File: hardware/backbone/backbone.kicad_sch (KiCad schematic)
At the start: 71 parts, among them J1 M20-7810645R, J140 M20-7810645R, J2 FROM_PREVIOUS, J3 M20-7810645R, J4 SM04B-SRSS-TB(LF)(SN), J5 FH12-24S-0.5SH(55), J9 TO NEXT, Q2 AO3401A, U1 ESP32-S3-WROOM-1_1U_FlexyPin_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, U10 ME6211C15M5G-N, U2 SN65HVD230DR, U3 HC-TYPE-C-16P-01A, U4 AP2112K-3.3TRG1, U5 AP2112K-3.3TRG1, U8 G3VM-61VY3, U9 ME6211C28M5G-N

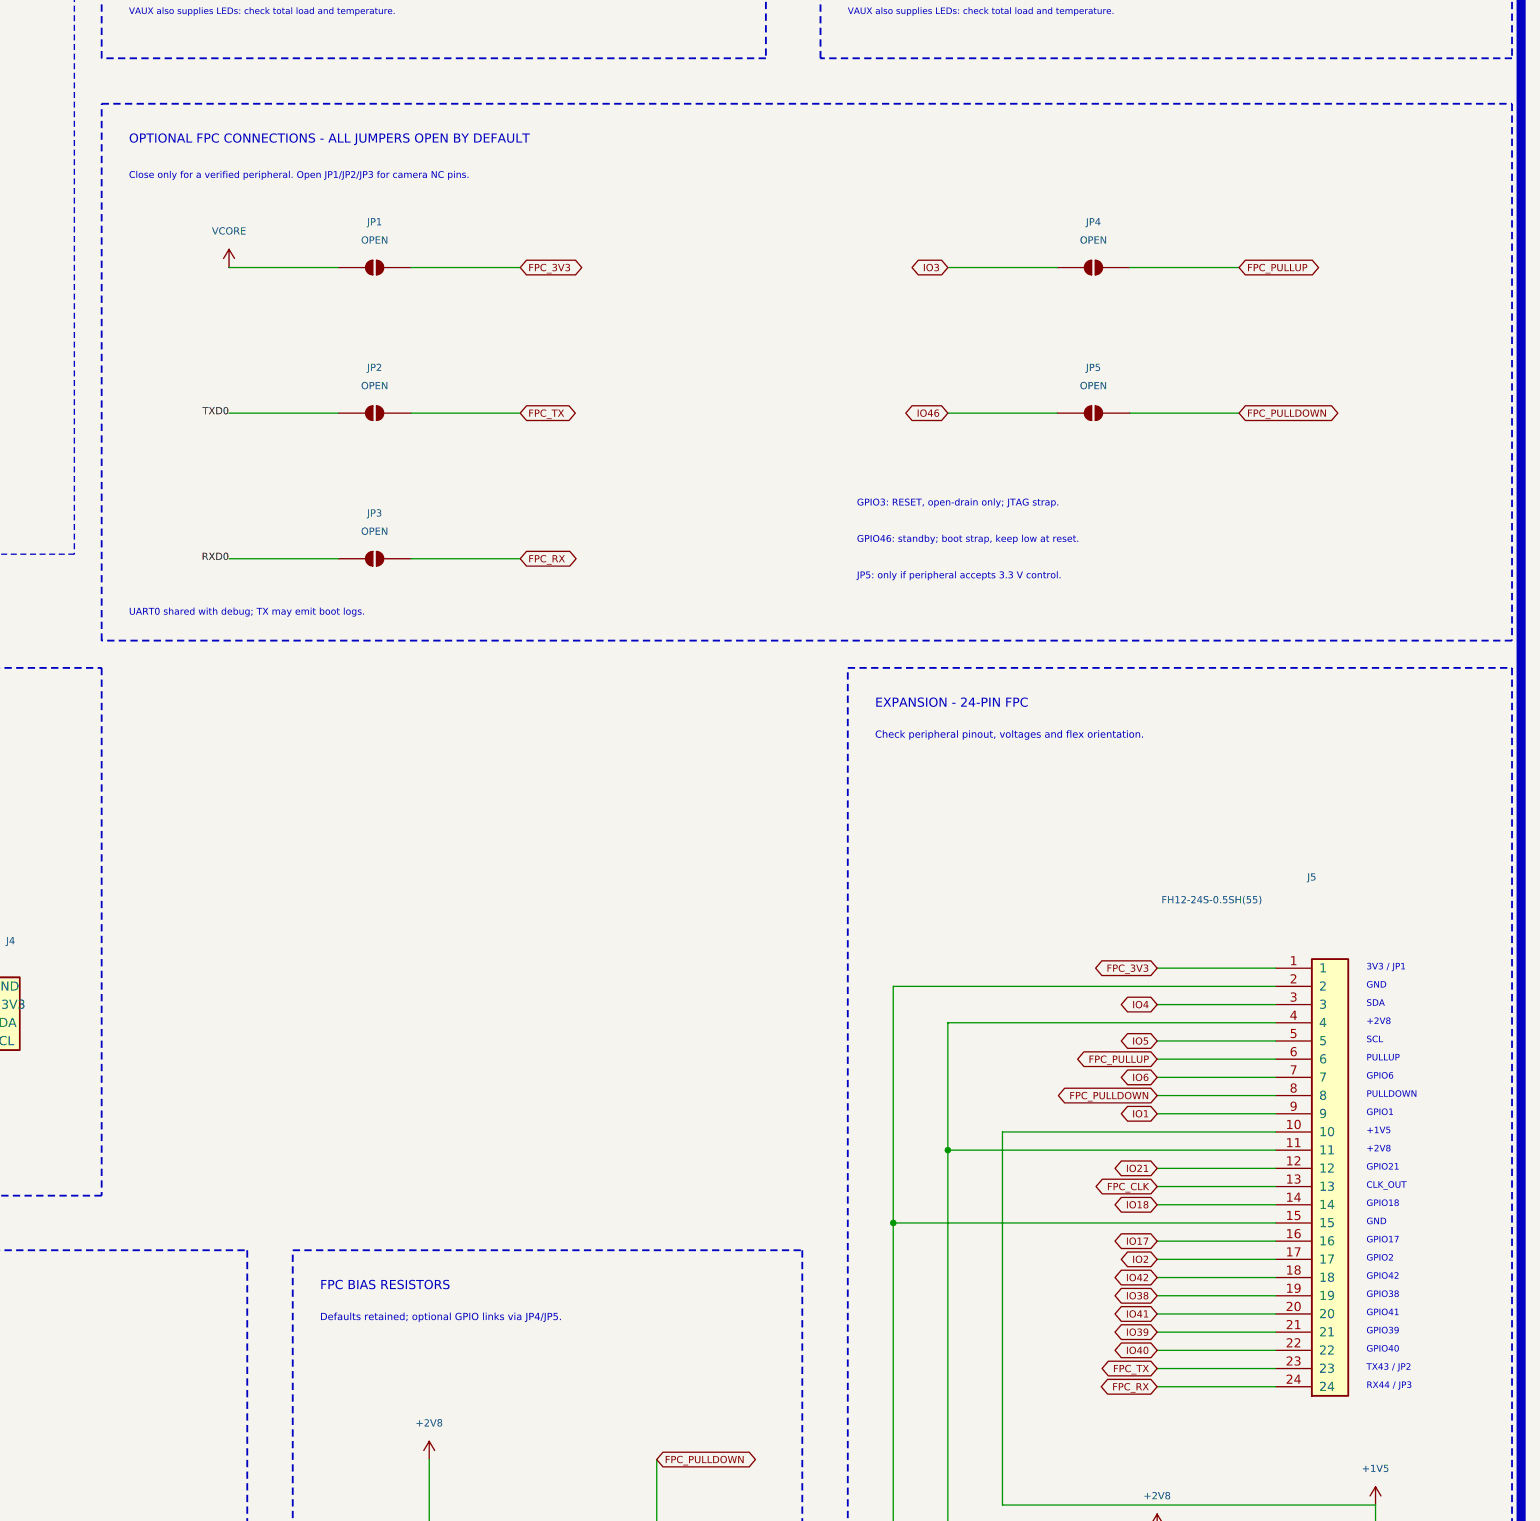
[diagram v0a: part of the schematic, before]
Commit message: Replace optional FPC solder jumpers with compact DNP zero-ohm links
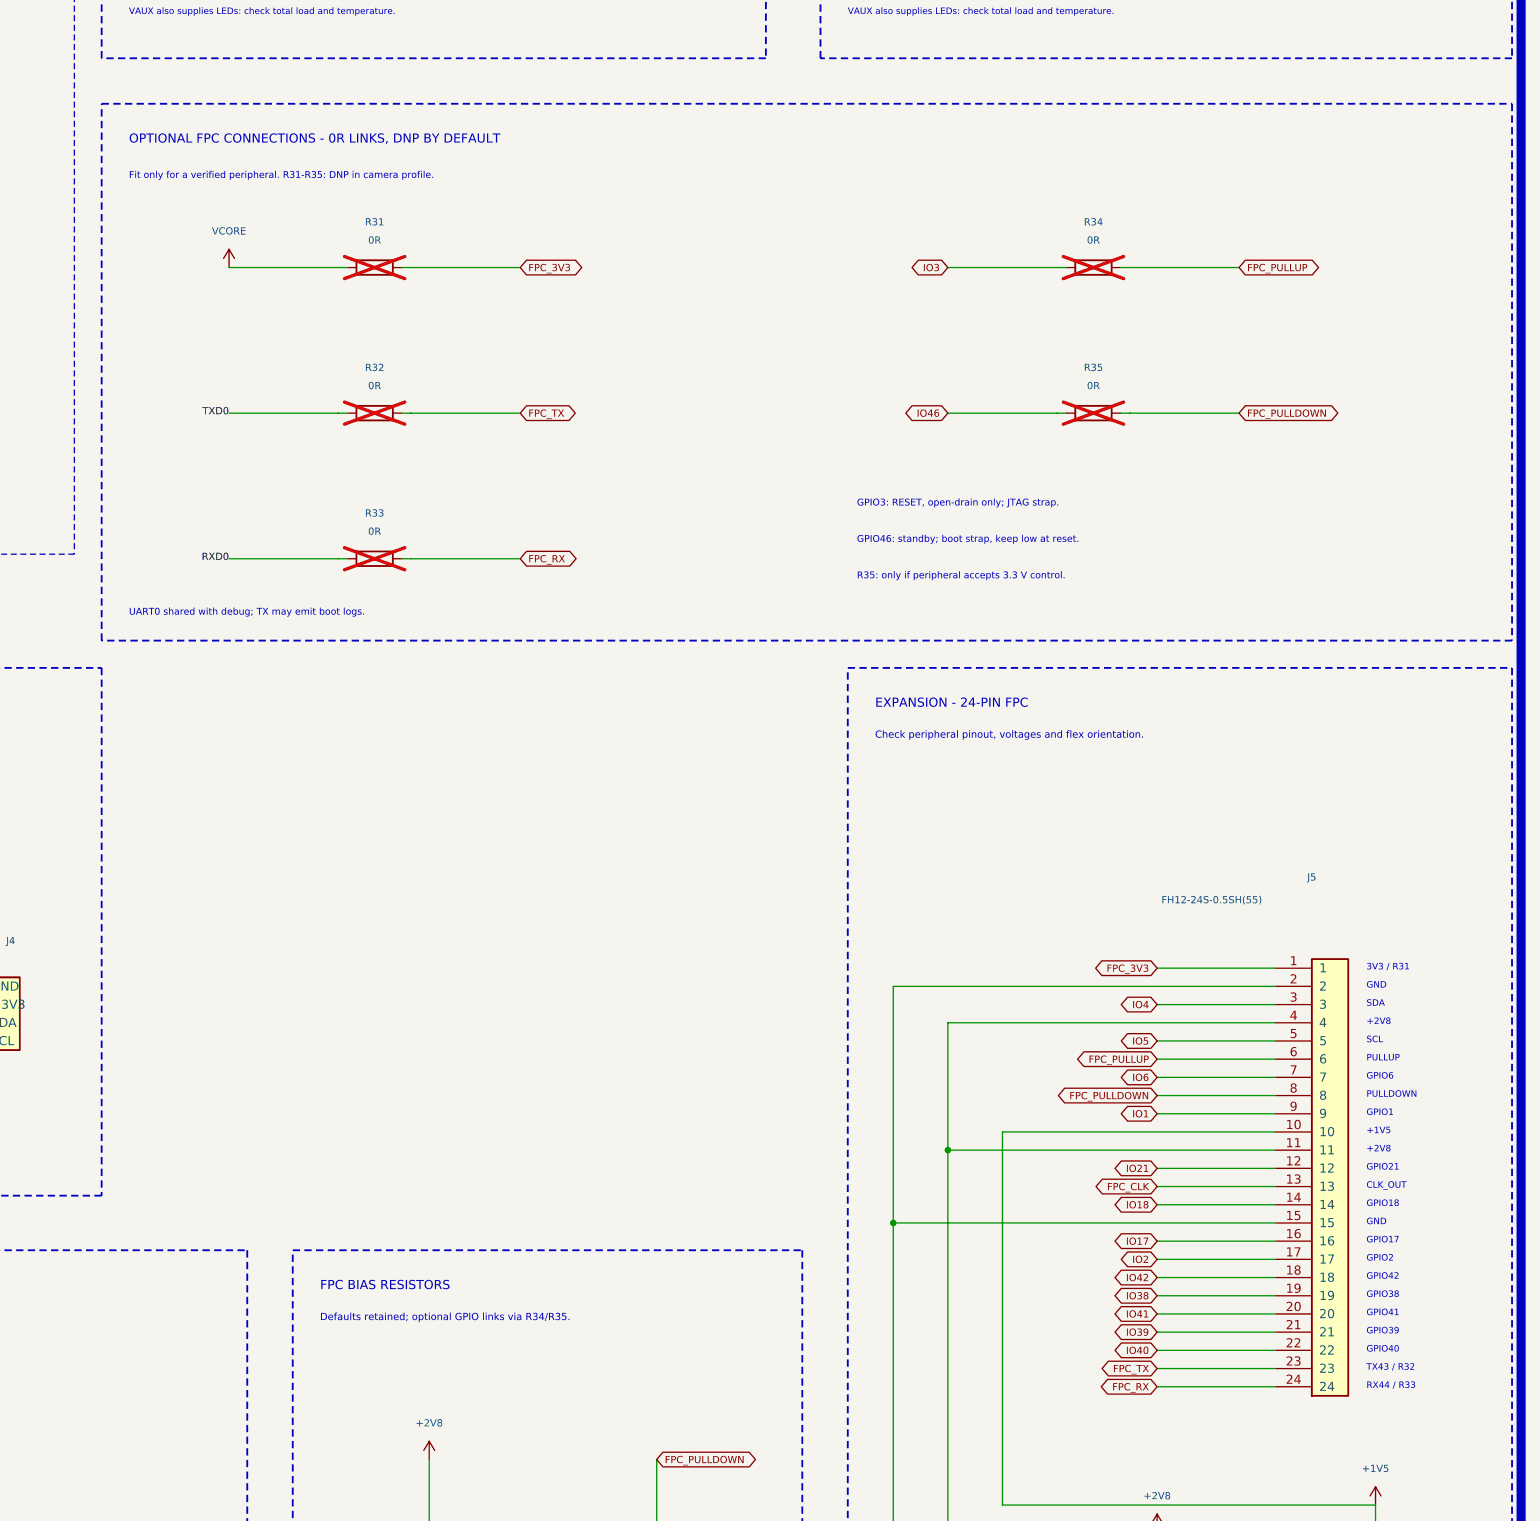
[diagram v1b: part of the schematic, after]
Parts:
- R31: renamed from JP1; value OPEN -> 0R; footprint Jumper:SolderJumper-2_P1.3mm_Open_Pad1.0x1.5mm -> Resistor_SMD:R_0402_1005Metric; symbol Jumper:SolderJumper_2_Open -> Device:R; now not fitted; now in the parts list
- R32: renamed from JP2; value OPEN -> 0R; footprint Jumper:SolderJumper-2_P1.3mm_Open_Pad1.0x1.5mm -> Resistor_SMD:R_0402_1005Metric; symbol Jumper:SolderJumper_2_Open -> Device:R; now not fitted; now in the parts list
- R33: renamed from JP3; value OPEN -> 0R; footprint Jumper:SolderJumper-2_P1.3mm_Open_Pad1.0x1.5mm -> Resistor_SMD:R_0402_1005Metric; symbol Jumper:SolderJumper_2_Open -> Device:R; now not fitted; now in the parts list
- R34: renamed from JP4; value OPEN -> 0R; footprint Jumper:SolderJumper-2_P1.3mm_Open_Pad1.0x1.5mm -> Resistor_SMD:R_0402_1005Metric; symbol Jumper:SolderJumper_2_Open -> Device:R; now not fitted; now in the parts list
- R35: renamed from JP5; value OPEN -> 0R; footprint Jumper:SolderJumper-2_P1.3mm_Open_Pad1.0x1.5mm -> Resistor_SMD:R_0402_1005Metric; symbol Jumper:SolderJumper_2_Open -> Device:R; now not fitted; now in the parts list
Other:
- note added: "3V3 / R31"
- note added: "Defaults retained; optional GPIO links via R34/R35."
- note added: "Fit only for a verified peripheral. R31-R35: DNP in camera profile."
- note added: "OPTIONAL FPC CONNECTIONS - 0R LINKS, DNP BY DEFAULT"
- note added: "R35: only if peripheral accepts 3.3 V control."
- note added: "RX44 / R33"
- note added: "TX43 / R32"
- note removed: "3V3 / JP1"
- note removed: "Close only for a verified peripheral. Open JP1/JP2/JP3 for camera NC pins."
- note removed: "Defaults retained; optional GPIO links via JP4/JP5."
- note removed: "JP5: only if peripheral accepts 3.3 V control."
- note removed: "OPTIONAL FPC CONNECTIONS - ALL JUMPERS OPEN BY DEFAULT"
- note removed: "RX44 / JP3"
- note removed: "TX43 / JP2"

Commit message: Use hand-solder 0603 links and document camera module compatibility
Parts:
- R31, R32, R33, R34, R35: footprint Resistor_SMD:R_0402_1005Metric -> Resistor_SMD:R_0603_1608Metric_Pad0.98x0.95mm_HandSolder
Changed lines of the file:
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@@
     )
   )
-  (property "Footprint" "Resistor_SMD:R_0402_1005Metric"
+  (property "Footprint" "Resistor_SMD:R_0603_1608Metric_Pad0.98x0.95mm_HandSolder"
     (at 420.37 124.46 0)
     (effects
@@
     )
   )
-  (property "Footprint" "Resistor_SMD:R_0402_1005Metric"
+  (property "Footprint" "Resistor_SMD:R_0603_1608Metric_Pad0.98x0.95mm_HandSolder"
     (at 420.37 144.78 0)
     (effects
@@
     )
   )
-  (property "Footprint" "Resistor_SMD:R_0402_1005Metric"
+  (property "Footprint" "Resistor_SMD:R_0603_1608Metric_Pad0.98x0.95mm_HandSolder"
     (at 420.37 165.1 0)
     (effects
@@
     )
   )
-  (property "Footprint" "Resistor_SMD:R_0402_1005Metric"
+  (property "Footprint" "Resistor_SMD:R_0603_1608Metric_Pad0.98x0.95mm_HandSolder"
     (at 520.7 124.46 0)
     (effects
@@
     )
   )
-  (property "Footprint" "Resistor_SMD:R_0402_1005Metric"
+  (property "Footprint" "Resistor_SMD:R_0603_1608Metric_Pad0.98x0.95mm_HandSolder"
     (at 520.7 144.78 0)
     (effects

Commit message: Update V3 LED layout for hand-formed MINI-E and solid FR4 windows
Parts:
- removed D4: SS54_C22452, SpaghettiLAB:SMA_L4.4-W2.8-LS5.4-R-RD, symbol SpaghettiLAB:SS54_C22452
- removed R20, R23: 5.1k, SpaghettiLAB:R0603, symbol Device:R
- removed USB1: TYPEC-324G-BCP24, SpaghettiLAB:USB-C-SMD_TYPEC-324G-BCP24, symbol SpaghettiLAB:TYPEC-324G-BCP24
- added D6: SS54_C22452, SpaghettiLAB:SMA_L4.4-W2.8-LS5.4-R-RD, symbol SpaghettiLAB:SS54_C22452
- added R22, R27: 5.1k, SpaghettiLAB:R0603, symbol Device:R
- LED1, LED2, LED3, LED4, LED5, LED6: value SK6805-EC15 -> SK6812MINI-E; footprint SpaghettiLABold:LED-SMD_4P-L1.5-W1.5-BL -> SpaghettiLAB:LED_SK6812MINI-E_FR4_Window_HandFormed; symbol SpaghettiLABold:SK6805-EC15 -> SpaghettiLAB:SK6812MINI-E_C5149201; LCSC Part C2890035 -> C5149201; MPN SK6805-EC15 -> SK6812MINI-E
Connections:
- net 5V: now also D6.2 (K)
- net ALED: now also LED1.2 (DIN); no longer LED1.1 (DIN)
- net GND: now also LED1.1 (GND), LED2.1 (GND), LED3.1 (GND), LED4.1 (GND), LED5.1 (GND), LED6.1 (GND), U3.1 (SHELL), U3.2 (SHELL), U3.3 (SHELL), U3.4 (SHELL), U3.A1B12 (GND), U3.B1A12 (GND), R22.2, R27.1; no longer LED1.4 (GND), LED2.4 (GND), LED3.4 (GND), LED4.4 (GND), LED5.4 (GND), LED6.4 (GND)
- net USB_D+: now also U3.A6 (D+), U3.B6 (D+)
- net USB_D-: now also U3.A7 (D-), U3.B7 (D-)
- net VAUX: now also LED1.3 (VDD), LED2.3 (VDD), LED3.3 (VDD), LED4.3 (VDD), LED5.3 (VDD), LED6.3 (VDD); no longer LED1.2 (VDD), LED2.2 (VDD), LED3.2 (VDD), LED4.2 (VDD), LED5.2 (VDD), LED6.2 (VDD)
- net VBUS: now also U3.A4B9 (VBUS), U3.B4A9 (VBUS), D6.1 (A)
- net at U3.A5 (CC1): now also R27.2
- net at U3.B5 (CC2): now also R22.1
- new net: LED1.4 (DOUT), LED2.2 (DIN)
- new net: LED2.4 (DOUT), LED3.2 (DIN)
- new net: LED3.4 (DOUT), LED4.2 (DIN)
- new net: LED4.4 (DOUT), LED5.2 (DIN)
- new net: LED5.4 (DOUT), LED6.2 (DIN)
- no-connect marks 16 -> 8
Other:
- moved on the sheet: H1, H2, H3, H4, R30, U3

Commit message: Update V3 power supply and dual-face magnetic edge contacts
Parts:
- removed C10, C6: 1uF, SpaghettiLAB:C0603, symbol Device:C
- removed U5: AP2112K-3.3TRG1, SpaghettiLAB:SOT-25-5_L2.9-W1.6-P0.95-LS2.8-BL, symbol SpaghettiLab:AP2112K-3.3TRG1
- added C84, C85: 100nF/50V, Capacitor_SMD:C_0603_1608Metric, symbol Device:C
- added C86: 22uF, Capacitor_SMD:C_0805_2012Metric, symbol Device:C
- added L1: 3.3uH, SpaghettiLAB:L_XRTC404012S, symbol Device:L
- added R36: 33k 1%, Resistor_SMD:R_0603_1608Metric, symbol Device:R
- added R37: 10k 1%, Resistor_SMD:R_0603_1608Metric, symbol Device:R
- C5, C9: value 1uF -> 22uF; footprint SpaghettiLAB:C0603 -> Capacitor_SMD:C_0805_2012Metric; LCSC Part (none) -> C45783; LCSC Part Name C128624 -> (none); MPN (none) -> CL21A226MAQNNNE
- J2: footprint Connector_PinSocket_2.54mm:PinSocket_1x05_P2.54mm_Horizontal -> SpaghettiLAB:Magnetic_J2_Edge_DualFace
- J9: footprint Connector_PinHeader_2.54mm:PinHeader_1x05_P2.54mm_Horizontal -> SpaghettiLAB:Magnetic_J9_Edge_DualFace
- U4: value AP2112K-3.3TRG1 -> TPS562201DDCR; footprint SpaghettiLAB:SOT-25-5_L2.9-W1.6-P0.95-LS2.8-BL -> SpaghettiLAB:TSOT-23-6_Power; symbol SpaghettiLab:AP2112K-3.3TRG1 -> SpaghettiLAB:TPS562201DDCR; LCSC Part C51118 -> C90061; LCSC Part Name C51118 -> (none); MANUFACTURER DIODES(美台) -> (none); MPN AP2112K-3.3TRG1 -> TPS562201DDCR
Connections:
- net VAUX is gone; now on net VCORE: C75.1, C77.1, LED1.3 (VDD), LED2.3 (VDD), LED3.3 (VDD), LED4.3 (VDD), LED5.3 (VDD), LED6.3 (VDD), U10.1 (V_{IN}), U10.3 (CE), U9.1 (V_{IN}), U9.3 (CE)
- net 5V: now also C5.1, U4.5 (EN), C85.1; no longer C5.2, U4.1 (VIN)
- net GND: now also C5.2, C9.2, U4.1 (GND), C85.2, C86.2, R37.2; no longer C5.1, C9.1, U4.2 (GND)
- net VCORE: now also C9.1, C86.1, L1.2, R36.1; no longer C9.2, U4.5 (VOUT)
- net at U4.4 (VFB): now also R36.2, R37.1
- new net: C84.2, L1.1, U4.2 (SW)
- new net: C84.1, U4.6 (VBST)
- no-connect marks 8 -> 6
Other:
- note added: "33k / 10k: nominal 3.302 V. Total load and thermal check required."
- note added: "Input: VCORE 3.3 V. Place capacitors close to the LDO."
- note added: "Keep VIN bypass, bootstrap and SW loop short."
- note added: "Shared 3.3 V: ESP32-S3, LEDs, peripherals and camera LDO inputs."
- note added: "VCORE also supplies LEDs: check total load and temperature."
- note added: "VCORE: 5 V TO 3.3 V / 2 A BUCK"
- note removed: "AUX SUPPLY"
- note removed: "CORE SUPPLY"
- note removed: "Input: VAUX 3.3 V. Place capacitors close to the LDO."
- note removed: "VAUX also supplies LEDs: check total load and temperature."
- moved on the sheet: C5, C9

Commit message: hardware: add configurable ports and LCSC component libraries
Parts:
- added C87: 100nF, SpaghettiLAB:C0603, symbol Device:C
- added unit 6 of J1
- added unit 2 of J1
- added unit 4 of J1
- added unit 5 of J1
- added unit 3 of J1
- added unit 5 of J140
- added unit 6 of J140
- added unit 3 of J140
- added unit 4 of J140
- added unit 2 of J140
- added Q3, Q4, Q5, Q6, Q7, Q8: AO6604, LCSC_Ports:SOT-23-6_L2.9-W1.6-P0.95-LS2.8-BL, symbol SpaghettiLAB:AO6604_TP
- added R38, R39, R40, R41, R42, R43, R44, R45, R46, R47, R48, R49: 100k, SpaghettiLAB:R0603, symbol Device:R
- added U11: XL9535QF24, LCSC_Ports:QFN-24_L4.0-W4.0-P0.50-BL-EP2.6, symbol SpaghettiLAB:XL9535QF24_6Ports
- J1, J140: symbol SpaghettiLAB:M20-7810645R -> SpaghettiLAB:M20-7810645R_6Ports; Check_prices https://www.snapeda.com/parts/M20-7810645R/Harwin/view-part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 -> (none); DigiKey_Part_Number 952-M20-7810645RCT-ND -> (none); MANUFACTURER HARWIN -> (none); MF Harwin -> (none); MP M20-7810645R -> (none); Package None -> (none); STANDARD Manufacturer Recommendations -> (none); SnapEDA_Link https://www.snapeda.com/parts/M20-7810645R/Harwin/view-part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 -> (none)
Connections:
- net A0: now also J1.1, J1.2, J140.1, J140.2, Q3.4 (D), Q3.6 (D)
- net A1: now also J1.3, J1.4, J140.3, J140.4, Q4.4 (D), Q4.6 (D)
- net A2: now also J1.5, J1.6, J140.5, J140.6, Q5.4 (D), Q5.6 (D)
- net A3: now also J1.7, J1.8, J140.7, J140.8, Q6.4 (D), Q6.6 (D)
- net A4: now also J1.10, J1.9, J140.10, J140.9, Q7.4 (D), Q7.6 (D)
- net A5: now also J1.11, J1.12, J140.11, J140.12, Q8.4 (D), Q8.6 (D)
- net GND: now also C87.2, Q3.5 (S), Q4.5 (S), Q5.5 (S), Q6.5 (S), Q7.5 (S), Q8.5 (S), R39.2, R41.2, R43.2, R45.2, R47.2, R49.2, U11.18 (A0), U11.23 (A1), U11.24 (A2), U11.25 (EPAD), U11.9 (GND)
- net IO4: now also U11.20 (SDA)
- net IO5: now also U11.19 (SCL)
- net VCORE: now also C87.1, Q3.2 (S), Q4.2 (S), Q5.2 (S), Q6.2 (S), Q7.2 (S), Q8.2 (S), R38.1, R40.1, R42.1, R44.1, R46.1, R48.1, U11.21 (VCC)
- new net: Q4.3 (G), R40.2, U11.3 (P02_/_P_GATE)
- new net: Q4.1 (G), R41.1, U11.4 (P03_/_N_GATE)
- new net: Q5.1 (G), R43.1, U11.6 (P05_/_N_GATE)
- new net: Q8.1 (G), R49.1, U11.13 (P13_/_N_GATE)
- new net: Q8.3 (G), R48.2, U11.12 (P12_/_P_GATE)
- new net: Q3.1 (G), R39.1, U11.2 (P01_/_N_GATE)
- new net: Q7.3 (G), R46.2, U11.10 (P10_/_P_GATE)
- new net: Q6.1 (G), R45.1, U11.8 (P07_/_N_GATE)
- new net: Q6.3 (G), R44.2, U11.7 (P06_/_P_GATE)
- new net: Q5.3 (G), R42.2, U11.5 (P04_/_P_GATE)
- new net: Q3.3 (G), R38.2, U11.1 (P00_/_P_GATE)
- new net: Q7.1 (G), R47.1, U11.11 (P11_/_N_GATE)
- no-connect marks 6 -> 11
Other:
- note added: "A0 / GPIO7 — FILA 1"
- note added: "A1 / GPIO8 — FILA 2"
- note added: "A2 / GPIO9 — FILA 3"
- note added: "A3 / GPIO10 — FILA 4"
- note added: "A4 / GPIO11 — FILA 5"
- note added: "A5 / GPIO12 — FILA 6"
- note added: "Firmware: prima GPIO in ingresso; spegnere entrambi i MOSFET prima di cambiare modo."
- note added: "IMPLEMENTATO: solo GPIO/3V3/GND. INA, shunt, DAC e lettura ADC dedicata rimandati."
- note added: "J1 e J140: coppie di contatti della stessa fila in comune. A6/A7 invariati."
- note added: "NON attivare P e N insieme. Questa revisione non aggiunge limitazione hardware."
- note added: "PORTE UNIVERSALI A0-A5 — BASE GPIO / 3V3 / GND"
- note added: "Q3-Q8: A=P-channel; B=N-channel. U11 A-F: comandi, G: alimentazione/I2C."
- note added: "U11: indirizzo I2C 0x20. Tutti i gate spenti al reset tramite pull-up P / pull-down N."
